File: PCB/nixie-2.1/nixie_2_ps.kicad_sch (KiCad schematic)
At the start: 20 parts, among them J1 Barrel_Jack_Switch, Q1 IRF730 TO220-3, U1 LM317_TO-220

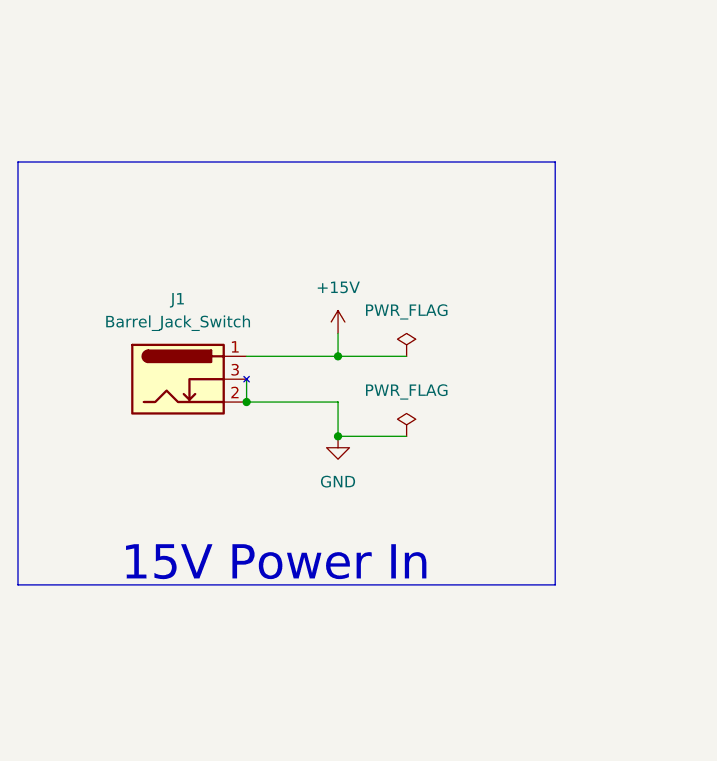
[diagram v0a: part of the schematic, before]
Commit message: updated z573M-logic - try using the zip version
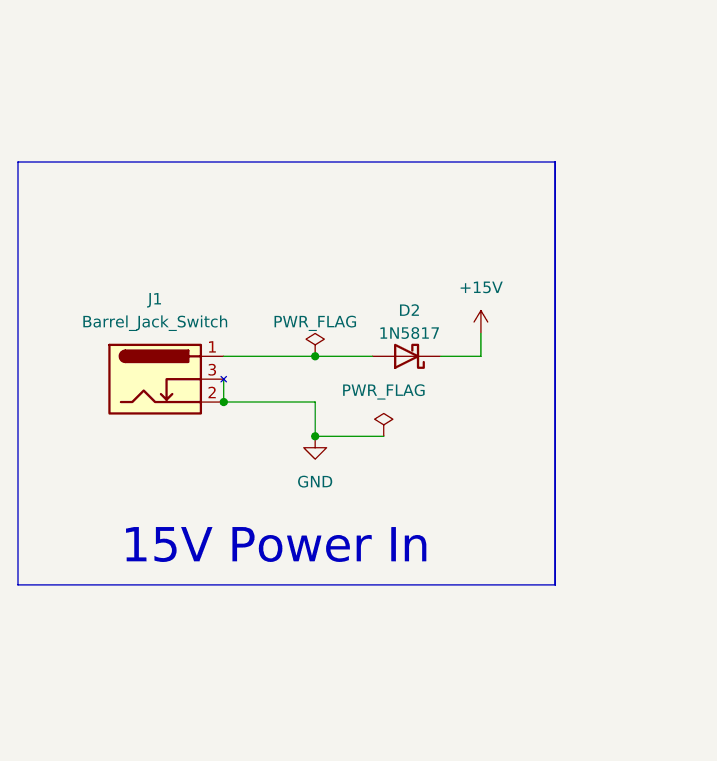
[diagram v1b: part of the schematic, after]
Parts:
- added D2: 1N5817, Diode_THT:D_DO-41_SOD81_P10.16mm_Horizontal, symbol Diode:1N5817
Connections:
- net +15V: now also D2.1 (K); no longer J1.1
- new net: D2.2 (A), J1.1
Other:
- moved on the sheet: J1
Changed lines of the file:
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@@
   (junction (at 161.29 53.34) (diameter 0) (color 0 0 0 0)
   )
-  (junction (at 49.53 99.06) (diameter 0) (color 0 0 0 0)
+  (junction (at 46.99 99.06) (diameter 0) (color 0 0 0 0)
   )
   (junction (at 147.32 45.72) (diameter 0) (color 0 0 0 0)
@@
   (junction (at 203.2 109.22) (diameter 0) (color 0 0 0 0)
   )
+  (junction (at 57.15 93.98) (diameter 0) (color 0 0 0 0)
+  )
   (junction (at 184.15 45.72) (diameter 0) (color 0 0 0 0)
   )
-  (junction (at 59.69 102.87) (diameter 0) (color 0 0 0 0)
+  (junction (at 57.15 102.87) (diameter 0) (color 0 0 0 0)
   )
   (junction (at 154.94 109.22) (diameter 0) (color 0 0 0 0)
@@
   (junction (at 153.67 45.72) (diameter 0) (color 0 0 0 0)
   )
-  (junction (at 59.69 93.98) (diameter 0) (color 0 0 0 0)
-  )
   (junction (at 168.91 45.72) (diameter 0) (color 0 0 0 0)
   )
@@
     (stroke (width 0) (type default))
   )
-  (wire (pts (xy 49.53 93.98) (xy 59.69 93.98))
-    (stroke (width 0) (type default))
-  )
   (wire (pts (xy 123.19 109.22) (xy 133.35 109.22))
     (stroke (width 0) (type default))
   )
-  (wire (pts (xy 59.69 102.87) (xy 67.31 102.87))
+  (wire (pts (xy 57.15 102.87) (xy 64.77 102.87))
     (stroke (width 0) (type default))
   )
@@
     (stroke (width 0) (type default))
   )
-  (wire (pts (xy 59.69 91.44) (xy 59.69 93.98))
+  (wire (pts (xy 57.15 93.98) (xy 63.5 93.98))
+    (stroke (width 0) (type default))
+  )
+  (wire (pts (xy 75.565 91.44) (xy 75.565 93.98))
     (stroke (width 0) (type default))
   )
@@
     (stroke (width 0) (type default))
   )
-  (wire (pts (xy 49.53 99.06) (xy 59.69 99.06))
+  (wire (pts (xy 46.99 99.06) (xy 57.15 99.06))
     (stroke (width 0) (type default))
   )
@@
     (stroke (width 0) (type default))
   )
-  (wire (pts (xy 59.69 93.98) (xy 67.31 93.98))
-    (stroke (width 0) (type default))
-  )
   (wire (pts (xy 170.18 109.22) (xy 180.34 109.22))
     (stroke (width 0) (type default))
@@
     (stroke (width 0) (type default))
   )
-  (polyline (pts (xy 83.82 72.39) (xy 83.82 119.38))
-    (stroke (width 0) (type default))
-  )
   (wire (pts (xy 168.91 33.02) (xy 168.91 45.72))
     (stroke (width 0) (type default))
@@
     (stroke (width 0) (type default))
   )
+  (wire (pts (xy 71.12 93.98) (xy 75.565 93.98))
+    (stroke (width 0) (type default))
+  )
   (wire (pts (xy 123.19 123.19) (xy 123.19 134.62))
     (stroke (width 0) (type default))
   )
-  (wire (pts (xy 49.53 96.52) (xy 49.53 99.06))
+  (wire (pts (xy 46.99 96.52) (xy 46.99 99.06))
     (stroke (width 0) (type default))
   )
@@
     (stroke (width 0) (type default))
   )
-  (wire (pts (xy 59.69 99.06) (xy 59.69 102.87))
+  (wire (pts (xy 57.15 99.06) (xy 57.15 102.87))
     (stroke (width 0) (type default))
   )
@@
     (stroke (width 0) (type default))
   )
+  (wire (pts (xy 46.99 93.98) (xy 57.15 93.98))
+    (stroke (width 0) (type default))
+  )
   (polyline (pts (xy 104.14 92.71) (xy 231.14 92.71))
     (stroke (width 0) (type default))
@@
   (wire (pts (xy 153.67 33.02) (xy 157.48 33.02))
     (stroke (width 0) (type default))
+  )
+  (rectangle (start 83.82 72.39) (end 83.82 119.38)
+    (stroke (width 0) (type default))
+    (fill (type none))
   )
   (text "5V Power Supply " (at 144.78 83.82 0)
@@
     (effects (font (size 3.81 3.81)) (justify left bottom))
   )
-  (text "15V Power In" (at 35.56 119.38 0)
+  (text "15V Power In" (at 35.56 117.475 0)
     (effects (font (size 3.81 3.81)) (justify left bottom))
   )
@@
     )
   )
-  (symbol (lib_id "power:PWR_FLAG") (at 67.31 93.98 0) (unit 1)
-    (in_bom yes) (on_board yes) (dnp no) (fields_autoplaced)
-    (property "Reference" "#FLG01" (at 67.31 92.075 0)
-      (effects (font (size 1.27 1.27)) hide)
-    )
-    (property "Value" "PWR_FLAG" (at 67.31 88.9 0)
-      (effects (font (size 1.27 1.27)))
-    )
-    (property "Footprint" "" (at 67.31 93.98 0)
-      (effects (font (size 1.27 1.27)) hide)
-    )
-    (property "Datasheet" "~" (at 67.31 93.98 0)
+  (symbol (lib_id "power:PWR_FLAG") (at 57.15 93.98 0) (unit 1)
+    (in_bom yes) (on_board yes) (dnp no)
+    (property "Reference" "#FLG01" (at 57.15 92.075 0)
+      (effects (font (size 1.27 1.27)) hide)
+    )
+    (property "Value" "PWR_FLAG" (at 57.15 90.17 0)
+      (effects (font (size 1.27 1.27)))
+    )
+    (property "Footprint" "" (at 57.15 93.98 0)
+      (effects (font (size 1.27 1.27)) hide)
+    )
+    (property "Datasheet" "~" (at 57.15 93.98 0)
       (effects (font (size 1.27 1.27)) hide)
     )
@@
     )
   )
-  (symbol (lib_id "power:PWR_FLAG") (at 67.31 102.87 0) (unit 1)
-    (in_bom yes) (on_board yes) (dnp no) (fields_autoplaced)
-    (property "Reference" "#FLG02" (at 67.31 100.965 0)
-      (effects (font (size 1.27 1.27)) hide)
-    )
-    (property "Value" "PWR_FLAG" (at 67.31 97.79 0)
-      (effects (font (size 1.27 1.27)))
-    )
-    (property "Footprint" "" (at 67.31 102.87 0)
-      (effects (font (size 1.27 1.27)) hide)
-    )
-    (property "Datasheet" "~" (at 67.31 102.87 0)
+  (symbol (lib_id "power:PWR_FLAG") (at 64.77 102.87 0) (unit 1)
+    (in_bom yes) (on_board yes) (dnp no) (fields_autoplaced)
+    (property "Reference" "#FLG02" (at 64.77 100.965 0)
+      (effects (font (size 1.27 1.27)) hide)
+    )
+    (property "Value" "PWR_FLAG" (at 64.77 97.79 0)
+      (effects (font (size 1.27 1.27)))
+    )
+    (property "Footprint" "" (at 64.77 102.87 0)
+      (effects (font (size 1.27 1.27)) hide)
+    )
+    (property "Datasheet" "~" (at 64.77 102.87 0)
       (effects (font (size 1.27 1.27)) hide)
     )
@@
     )
   )
-  (symbol (lib_id "power:+15V") (at 59.69 91.44 0) (unit 1)
-    (in_bom yes) (on_board yes) (dnp no) (fields_autoplaced)
-    (property "Reference" "#PWR012" (at 59.69 95.25 0)
-      (effects (font (size 1.27 1.27)) hide)
-    )
-    (property "Value" "+15V" (at 59.69 86.36 0)
-      (effects (font (size 1.27 1.27)))
-    )
-    (property "Footprint" "" (at 59.69 91.44 0)
-      (effects (font (size 1.27 1.27)) hide)
-    )
-    (property "Datasheet" "" (at 59.69 91.44 0)
+  (symbol (lib_id "power:+15V") (at 75.565 91.44 0) (unit 1)
+    (in_bom yes) (on_board yes) (dnp no) (fields_autoplaced)
+    (property "Reference" "#PWR012" (at 75.565 95.25 0)
+      (effects (font (size 1.27 1.27)) hide)
+    )
+    (property "Value" "+15V" (at 75.565 86.36 0)
+      (effects (font (size 1.27 1.27)))
+    )
+    (property "Footprint" "" (at 75.565 91.44 0)
+      (effects (font (size 1.27 1.27)) hide)
+    )
+    (property "Datasheet" "" (at 75.565 91.44 0)
       (effects (font (size 1.27 1.27)) hide)
     )
@@
     )
   )
-  (symbol (lib_id "power:GND") (at 59.69 102.87 0) (unit 1)
-    (in_bom yes) (on_board yes) (dnp no) (fields_autoplaced)
-    (property "Reference" "#PWR013" (at 59.69 109.22 0)
-      (effects (font (size 1.27 1.27)) hide)
-    )
-    (property "Value" "GND" (at 59.69 107.95 0)
-      (effects (font (size 1.27 1.27)))
-    )
-    (property "Footprint" "" (at 59.69 102.87 0)
-      (effects (font (size 1.27 1.27)) hide)
-    )
-    (property "Datasheet" "" (at 59.69 102.87 0)
+  (symbol (lib_id "power:GND") (at 57.15 102.87 0) (unit 1)
+    (in_bom yes) (on_board yes) (dnp no) (fields_autoplaced)
+    (property "Reference" "#PWR013" (at 57.15 109.22 0)
+      (effects (font (size 1.27 1.27)) hide)
+    )
+    (property "Value" "GND" (at 57.15 107.95 0)
+      (effects (font (size 1.27 1.27)))
+    )
+    (property "Footprint" "" (at 57.15 102.87 0)
+      (effects (font (size 1.27 1.27)) hide)
+    )
+    (property "Datasheet" "" (at 57.15 102.87 0)
       (effects (font (size 1.27 1.27)) hide)
     )
@@
         (path "/a160f91f-03e0-4279-9371-b79f1f206693/307d414c-e906-4581-9ece-da89ba708596"
           (reference "#PWR013") (unit 1)
+        )
+      )
+    )
+  )
+  (symbol (lib_id "Diode:1N5817") (at 67.31 93.98 180) (unit 1)
+    (in_bom yes) (on_board yes) (dnp no) (fields_autoplaced)
+    (property "Reference" "D2" (at 67.6275 88.9 0)
+      (effects (font (size 1.27 1.27)))
+    )
+    (property "Value" "1N5817" (at 67.6275 91.44 0)
+      (effects (font (size 1.27 1.27)))
+    )
+    (property "Footprint" "Diode_THT:D_DO-41_SOD81_P10.16mm_Horizontal" (at 67.31 89.535 0)
+      (effects (font (size 1.27 1.27)) hide)
+    )
+    (property "Datasheet" "http://www.vishay.com/docs/88525/1n5817.pdf" (at 67.31 93.98 0)
+      (effects (font (size 1.27 1.27)) hide)
+    )
+    (pin "1")
+    (pin "2")
+    (instances
+      (project "nixie-2.1"
+        (path "/a160f91f-03e0-4279-9371-b79f1f206693/307d414c-e906-4581-9ece-da89ba708596"
+          (reference "D2") (unit 1)
         )
       )
@@
     )
   )
-  (symbol (lib_id "Connector:Barrel_Jack_Switch") (at 41.91 96.52 0) (unit 1)
-    (in_bom yes) (on_board yes) (dnp no) (fields_autoplaced)
-    (property "Reference" "J1" (at 41.91 87.63 0)
-      (effects (font (size 1.27 1.27)))
-    )
-    (property "Value" "Barrel_Jack_Switch" (at 41.91 90.17 0)
-      (effects (font (size 1.27 1.27)))
-    )
-    (property "Footprint" "nixie-2.1-footprints:BarrelJack_Horizontal" (at 43.18 97.536 0)
-      (effects (font (size 1.27 1.27)) hide)
-    )
-    (property "Datasheet" "~" (at 43.18 97.536 0)
-      (effects (font (size 1.27 1.27)) hide)
-    )
+  (symbol (lib_id "Connector:Barrel_Jack_Switch") (at 39.37 96.52 0) (unit 1)
+    (in_bom yes) (on_board yes) (dnp no) (fields_autoplaced)
+    (property "Reference" "J1" (at 39.37 87.63 0)
+      (effects (font (size 1.27 1.27)))
+    )
+    (property "Value" "Barrel_Jack_Switch" (at 39.37 90.17 0)
+      (effects (font (size 1.27 1.27)))
+    )
+    (property "Footprint" "nixie-2.1-footprints:BarrelJack_Horizontal" (at 40.64 97.536 0)
+      (effects (font (size 1.27 1.27)) hide)
+    )
+    (property "Datasheet" "~" (at 40.64 97.536 0)
+      (effects (font (size 1.27 1.27)) hide)
+    )
